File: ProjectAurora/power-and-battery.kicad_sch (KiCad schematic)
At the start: 18 parts, among them IC3 BQ25185DLHR, IC4 MAX17048G+T10, IC5 TPS63900DSKR

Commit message: Starting Layout
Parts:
- BT1: footprint (none) -> Connector_JST:JST_SH_SM02B-SRSS-TB_1x02-1MP_P1.00mm_Horizontal
- C20, C21, C22, C23, C24, C25: footprint (none) -> Capacitor_SMD:C_0603_1608Metric
- IC3: footprint SON40P220X200X80-11N -> Package_DFN_QFN:Texas_DLH0010A_WSON-10-1EP_2.2x2mm_P0.4mm_EP0.9x1.5mm_ThermalVias
- IC4: footprint SON50P200X200X80-9N-D -> Package_DFN_QFN:TDFN-8-1EP_2x2mm_P0.5mm_EP0.8x1.2mm
- IC5: footprint SON50P250X250X80-11N-D -> Package_SON:WSON-10-1EP_2.5x2.5mm_P0.5mm_EP1.2x2mm
- L1: footprint (none) -> Inductor_SMD:L_Coilcraft_0805HQ_2012Metric
- R14, R15, R16, R17, R18, R21, TH1: footprint (none) -> Resistor_SMD:R_0603_1608Metric
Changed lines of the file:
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@@
 			)
 		)
-		(property "Footprint" ""
+		(property "Footprint" "Capacitor_SMD:C_0603_1608Metric"
 			(at 70.8152 82.55 0)
 			(effects
@@
 			)
 		)
-		(property "Footprint" "SON50P250X250X80-11N-D"
+		(property "Footprint" "Package_SON:WSON-10-1EP_2.5x2.5mm_P0.5mm_EP1.2x2mm"
 			(at 184.15 207.95 0)
 			(effects
@@
 			)
 		)
-		(property "Footprint" ""
+		(property "Footprint" "Resistor_SMD:R_0603_1608Metric"
 			(at 106.172 137.16 90)
 			(effects
@@
 			)
 		)
-		(property "Footprint" ""
+		(property "Footprint" "Capacitor_SMD:C_0603_1608Metric"
 			(at 119.0752 82.55 0)
 			(effects
@@
 			)
 		)
-		(property "Footprint" ""
+		(property "Footprint" "Connector_JST:JST_SH_SM02B-SRSS-TB_1x02-1MP_P1.00mm_Horizontal"
 			(at 43.18 88.646 90)
 			(effects
@@
 			)
 		)
-		(property "Footprint" ""
+		(property "Footprint" "Resistor_SMD:R_0603_1608Metric"
 			(at 114.3 89.408 90)
 			(effects
@@
 			)
 		)
-		(property "Footprint" ""
+		(property "Footprint" "Resistor_SMD:R_0603_1608Metric"
 			(at 114.3 91.948 90)
 			(effects
@@
 			)
 		)
-		(property "Footprint" ""
+		(property "Footprint" "Resistor_SMD:R_0603_1608Metric"
 			(at 110.49 99.06 0)
 			(effects
@@
 			)
 		)
-		(property "Datasheet" "~"
+		(property "Datasheet" "https://jlcpcb.com/api/file/downloadByFileSystemAccessId/8588919985616138240"
 			(at 110.49 99.06 0)
 			(effects
@@
 			)
 		)
-		(property "Footprint" ""
+		(property "Footprint" "Capacitor_SMD:C_0603_1608Metric"
 			(at 195.2752 113.03 0)
 			(effects
@@
 			)
 		)
-		(property "Footprint" ""
+		(property "Footprint" "Inductor_SMD:L_Coilcraft_0805HQ_2012Metric"
 			(at 198.12 118.11 0)
 			(effects
@@
 			)
 		)
-		(property "Datasheet" "~"
+		(property "Datasheet" "https://jlcpcb.com/api/file/downloadByFileSystemAccessId/8586176145175810048"
 			(at 198.12 118.11 0)
 			(effects
@@
 			)
 		)
-		(property "Footprint" "SON40P220X200X80-11N"
+		(property "Footprint" "Package_DFN_QFN:Texas_DLH0010A_WSON-10-1EP_2.2x2mm_P0.4mm_EP0.9x1.5mm_ThermalVias"
 			(at 106.68 177.47 0)
 			(effects
@@
 			)
 		)
-		(property "Footprint" "SON50P200X200X80-9N-D"
+		(property "Footprint" "Package_DFN_QFN:TDFN-8-1EP_2x2mm_P0.5mm_EP0.8x1.2mm"
 			(at 96.52 220.65 0)
 			(effects
@@
 			)
 		)
-		(property "Footprint" ""
+		(property "Footprint" "Capacitor_SMD:C_0603_1608Metric"
 			(at 195.2752 123.19 0)
 			(effects
@@
 			)
 		)
-		(property "Footprint" ""
+		(property "Footprint" "Capacitor_SMD:C_0603_1608Metric"
 			(at 49.2252 92.71 0)
 			(effects
@@
 			)
 		)
-		(property "Footprint" ""
+		(property "Footprint" "Capacitor_SMD:C_0603_1608Metric"
 			(at 55.5752 138.43 0)
 			(effects
@@
 			)
 		)
-		(property "Footprint" ""
+		(property "Footprint" "Resistor_SMD:R_0603_1608Metric"
 			(at 127.762 88.9 90)
 			(effects
@@
 			)
 		)
-		(property "Footprint" ""
+		(property "Footprint" "Resistor_SMD:R_0603_1608Metric"
 			(at 153.67 119.888 90)
 			(effects
@@
 			)
 		)
-		(property "Footprint" ""
+		(property "Footprint" "Resistor_SMD:R_0603_1608Metric"
 			(at 62.992 91.44 90)
 			(effects

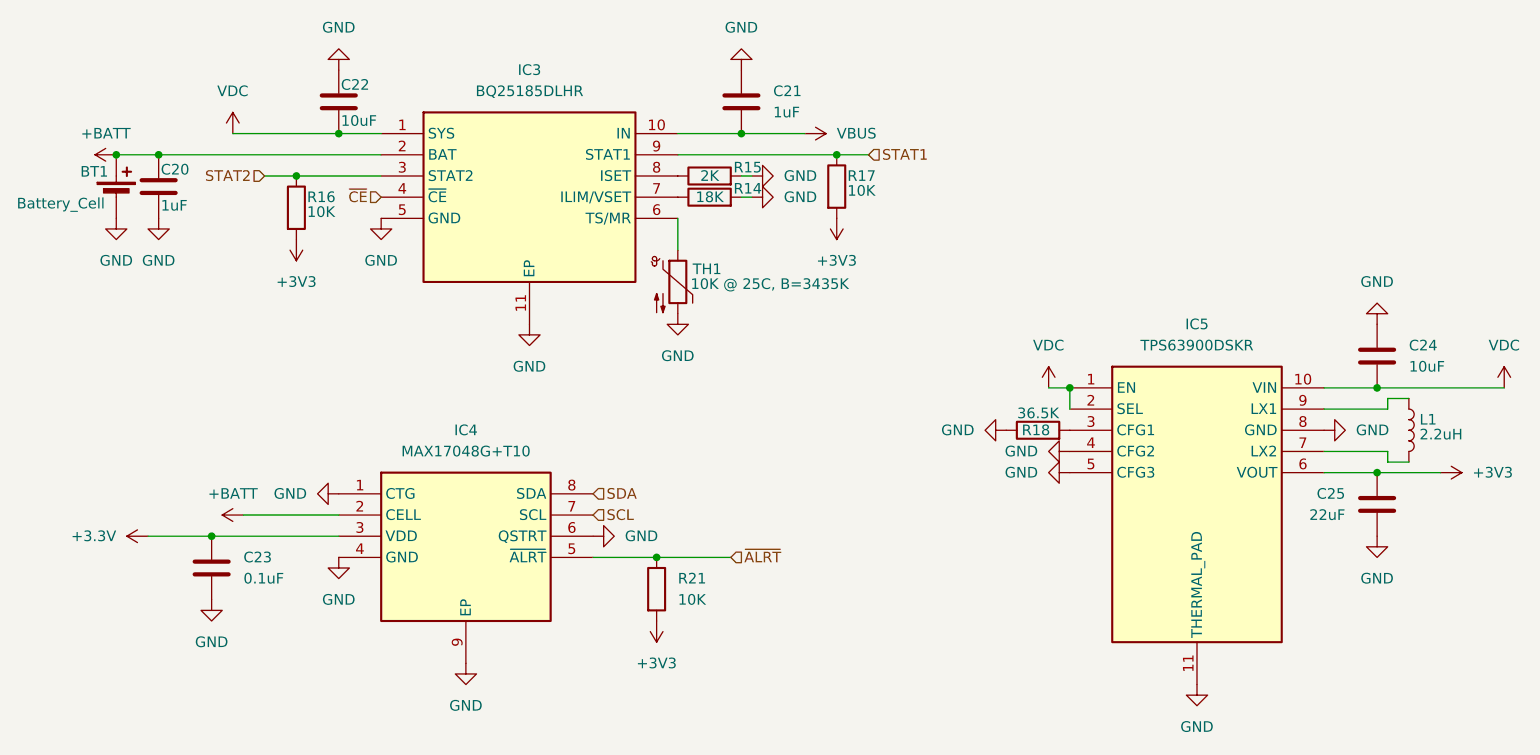
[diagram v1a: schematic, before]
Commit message: Prototype Board Layout Done
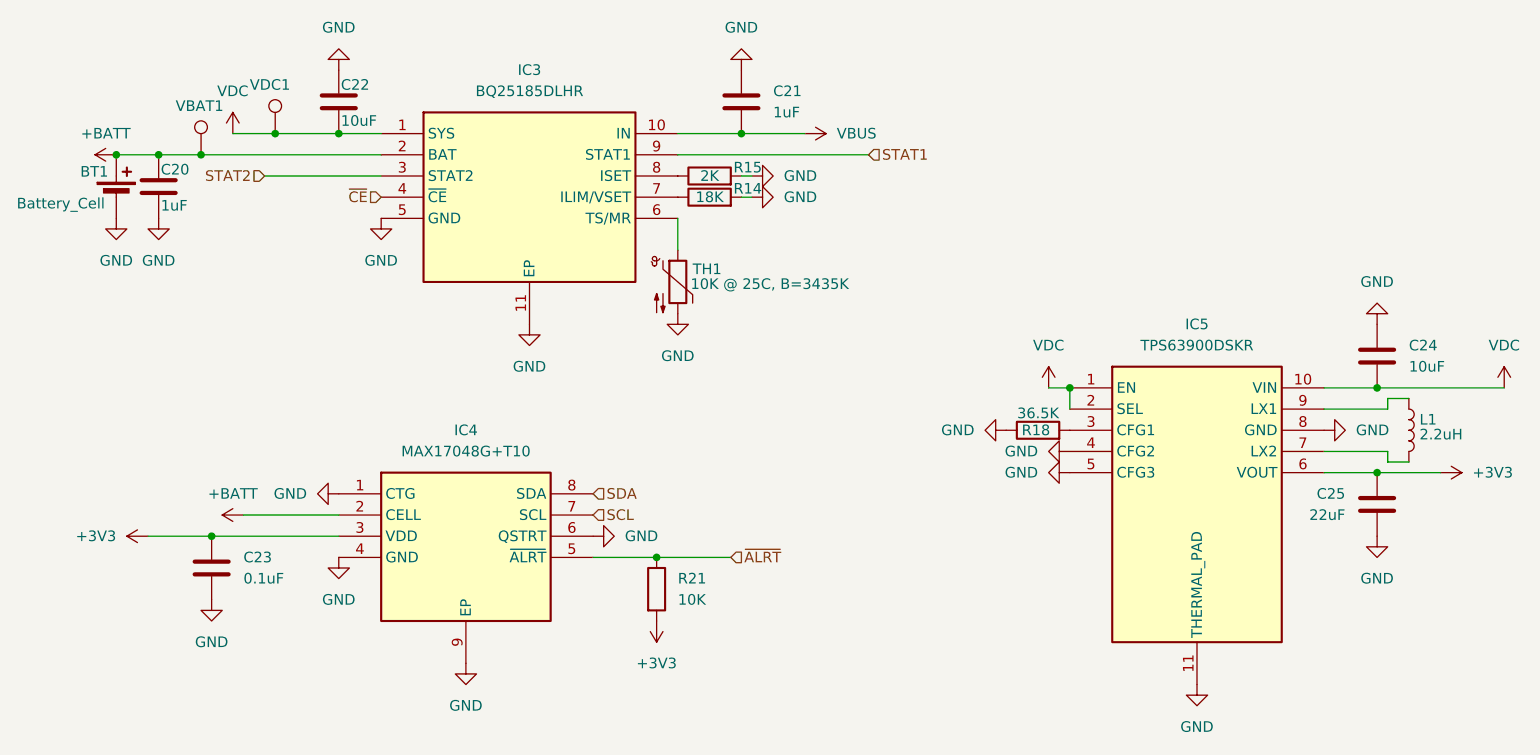
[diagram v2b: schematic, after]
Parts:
- removed R16, R17: 10K, Resistor_SMD:R_0603_1608Metric, symbol Device:R
- added VBAT1, VDC1: TestPoint, TestPoint:TestPoint_Pad_1.0x1.0mm, symbol Connector:TestPoint
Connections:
- net +3.3V is gone; now on net +3V3: C23.1, IC4.3 (VDD)
- net +BATT: now also VBAT1.1
- net VDC: now also VDC1.1
